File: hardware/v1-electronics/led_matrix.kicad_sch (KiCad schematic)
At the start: 84 parts

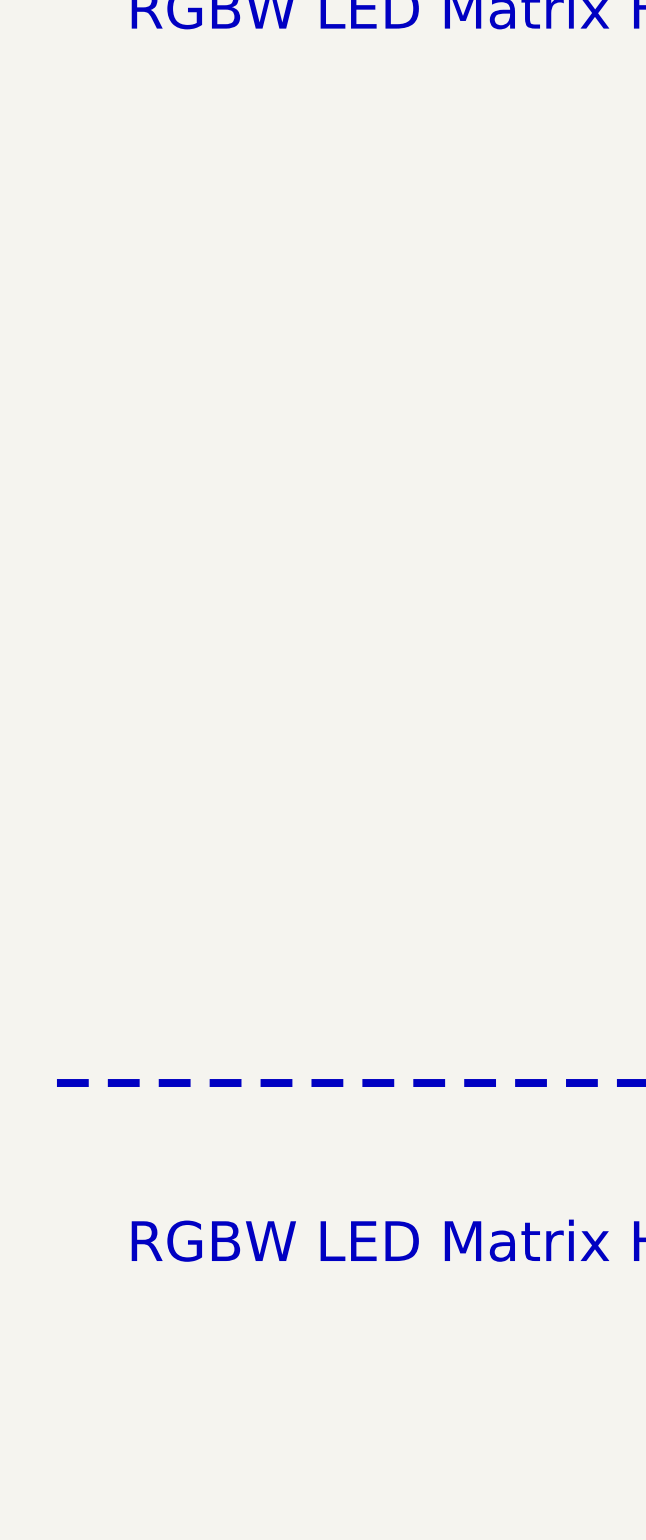
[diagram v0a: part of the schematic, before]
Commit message: refactor(v1 hardware): root level schematic is made discriptive with hierarchical pins
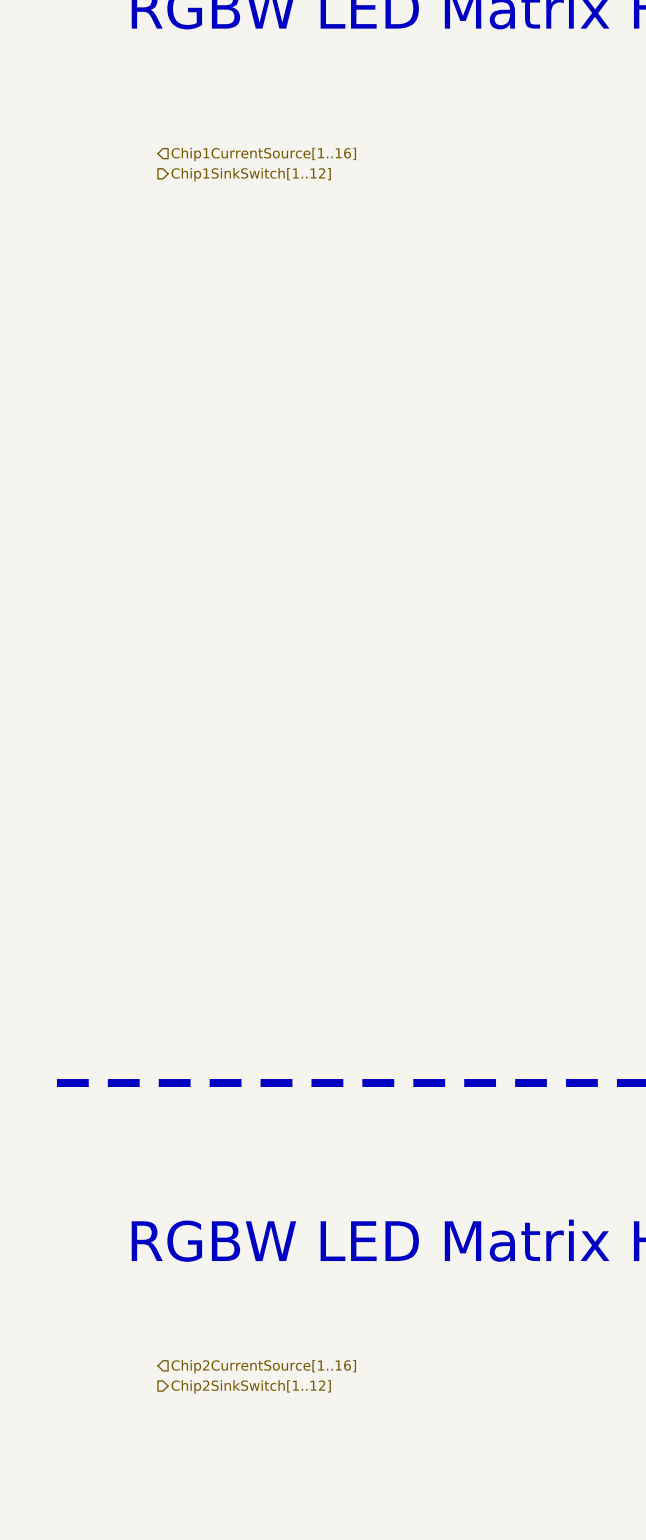
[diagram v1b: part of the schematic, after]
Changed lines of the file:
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@@
+		)
+	)
+	(hierarchical_label "Chip2SinkSwitch[1..12]"
+		(shape output)
+		(at 25.4 205.74 0)
+		(effects
+			(font
+				(size 1.27 1.27)
+			)
+			(justify left)
 		)
 	)
@@
 		)
 	)
+	(hierarchical_label "Chip2CurrentSource[1..16]"
+		(shape input)
+		(at 25.4 203.2 0)
+		(effects
+			(font
+				(size 1.27 1.27)
+			)
+			(justify left)
+		)
+	)
 	(hierarchical_label "CS4_2"
 		(shape input)
@@
 		)
 	)
+	(hierarchical_label "Chip1CurrentSource[1..16]"
+		(shape input)
+		(at 25.4 50.8 0)
+		(effects
+			(font
+				(size 1.27 1.27)
+			)
+			(justify left)
+		)
+	)
 	(hierarchical_label "CS2_1"
 		(shape input)
@@
 		)
 	)
+	(hierarchical_label "Chip1SinkSwitch[1..12]"
+		(shape output)
+		(at 25.4 53.34 0)
+		(effects
+			(font
+				(size 1.27 1.27)
+			)
+			(justify left)
+		)
+	)

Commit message: refactor(v1 hardware): transition to hierarchical pins complete
All the buses renamed to stuff
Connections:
- net CS10_1 renamed Chip1CurrentSource10
- net CS10_2 renamed Chip2CurrentSource10
- net CS11_1 renamed Chip1CurrentSource11
- net CS11_2 renamed Chip2CurrentSource11
- net CS12_1 renamed Chip1CurrentSource12
- net CS12_2 renamed Chip2CurrentSource12
- net CS13_1 renamed Chip1CurrentSource13
- net CS13_2 renamed Chip2CurrentSource13
- net CS14_1 renamed Chip1CurrentSource14
- net CS14_2 renamed Chip2CurrentSource14
- net CS15_1 renamed Chip1CurrentSource15
- net CS15_2 renamed Chip2CurrentSource15
- net CS16_1 renamed Chip1CurrentSource16
- net CS16_2 renamed Chip2CurrentSource16
- net CS1_1 renamed Chip1CurrentSource1
- net CS1_2 renamed Chip2CurrentSource1
- net CS2_1 renamed Chip1CurrentSource2
- net CS2_2 renamed Chip2CurrentSource2
- net CS3_1 renamed Chip1CurrentSource3
- net CS3_2 renamed Chip2CurrentSource3
- net CS4_1 renamed Chip1CurrentSource4
- net CS4_2 renamed Chip2CurrentSource4
- net CS5_1 renamed Chip1CurrentSource5
- net CS5_2 renamed Chip2CurrentSource5
- net CS6_1 renamed Chip1CurrentSource6
- net CS6_2 renamed Chip2CurrentSource6
- net CS7_1 renamed Chip1CurrentSource7
- net CS7_2 renamed Chip2CurrentSource7
- net CS8_1 renamed Chip1CurrentSource8
- net CS8_2 renamed Chip2CurrentSource8
- net CS9_1 renamed Chip1CurrentSource9
- net CS9_2 renamed Chip2CurrentSource9
- net SW10_G_1 renamed Chip1SinkSwitch10
- net SW10_G_2 renamed Chip2SinkSwitch10
- net SW11_R_1 renamed Chip1SinkSwitch11
- net SW11_R_2 renamed Chip2SinkSwitch11
- net SW12_W_1 renamed Chip1SinkSwitch12
- net SW12_W_2 renamed Chip2SinkSwitch12
- net SW1_B_1 renamed Chip1SinkSwitch1
- net SW1_B_2 renamed Chip2SinkSwitch1
- net SW2_G_1 renamed Chip1SinkSwitch2
- net SW2_G_2 renamed Chip2SinkSwitch2
- net SW3_R_1 renamed Chip1SinkSwitch3
- net SW3_R_2 renamed Chip2SinkSwitch3
- net SW4_W_1 renamed Chip1SinkSwitch4
- net SW4_W_2 renamed Chip2SinkSwitch4
- net SW5_B_1 renamed Chip1SinkSwitch5
- net SW5_B_2 renamed Chip2SinkSwitch5
- net SW6_G_1 renamed Chip1SinkSwitch6
- net SW6_G_2 renamed Chip2SinkSwitch6
- net SW7_R_1 renamed Chip1SinkSwitch7
- net SW7_R_2 renamed Chip2SinkSwitch7
- net SW8_W_1 renamed Chip1SinkSwitch8
- net SW8_W_2 renamed Chip2SinkSwitch8
- net SW9_B_1 renamed Chip1SinkSwitch9
- net SW9_B_2 renamed Chip2SinkSwitch9
- no-connect marks 0 -> 24
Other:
- note added: "Blue"
- note added: "Green"
- note added: "Red"
- note added: "White"

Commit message: refactor(v1 hardware): refactored led controllers into a seperate sheet
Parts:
- added JP1: Jumper_2_Open, symbol Jumper:Jumper_2_Open
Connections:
- new net LED Matrix Controller 1/SYNC: JP1.1 (A)
- new net LED Matrix Controller 2/SYNC: JP1.2 (B)
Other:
- added sheet LED Matrix Controller 1 (matric_controller_1.kicad_sch)
- added sheet LED Matrix Controller 2 (matrix_controller_2.kicad_sch)

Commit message: refactor(v1 hardware): get references in order
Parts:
- renumbered LED1_1 to LED1, LED33_2 to LED10, LED2_2 to LED11, LED18_2 to LED12, LED34_2 to LED13, LED3_2 to LED14, LED19_1 to LED15, LED35_1 to LED16, LED4_1 to LED17, LED20_1 to LED18, LED36_1 to LED19, LED17_1 to LED2, LED5_1 to LED20, LED21_1 to LED21, LED19_2 to LED22, LED35_2 to LED23, LED4_2 to LED24, LED20_2 to LED25, LED36_2 to LED26, LED5_2 to LED27, LED21_2 to LED28, LED37_1 to LED29, LED33_1 to LED3, LED6_1 to LED30, LED22_1 to LED31, LED38_1 to LED32, LED7_1 to LED33, LED23_1 to LED34, LED39_1 to LED35, LED37_2 to LED36, LED6_2 to LED37, LED22_2 to LED38, LED38_2 to LED39, LED2_1 to LED4, LED7_2 to LED40, LED23_2 to LED41, LED39_2 to LED42, LED8_1 to LED43, LED24_1 to LED44, LED40_1 to LED45, LED9_1 to LED46, LED25_1 to LED47, LED41_1 to LED48, LED10_1 to LED49, LED18_1 to LED5, LED8_2 to LED50, LED24_2 to LED51, LED40_2 to LED52, LED9_2 to LED53, LED25_2 to LED54, LED41_2 to LED55, LED10_2 to LED56, LED26_1 to LED57, LED42_1 to LED58, LED11_1 to LED59, LED34_1 to LED6, LED27_1 to LED60, LED16_1 to LED61, LED12_1 to LED62, LED28_1 to LED63, LED26_2 to LED66, LED42_2 to LED67, LED11_2 to LED68, LED27_2 to LED69, LED3_1 to LED7, LED16_2 to LED70, LED12_2 to LED71, LED28_2 to LED72, LED32_1 to LED73, LED13_1 to LED74, LED29_1 to LED75, LED15_1 to LED76, LED14_1 to LED77, LED30_1 to LED78, LED31_1 to LED79, LED1_2 to LED8, LED32_2 to LED80, LED13_2 to LED81, LED29_2 to LED82, LED31_2 to LED83, LED14_2 to LED84, LED30_2 to LED85, LED15_2 to LED86, LED17_2 to LED9
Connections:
- net Chip1CurrentSource12: now also LED73.5 (ANODE)
- net Chip1CurrentSource13: now also LED76.5 (ANODE)
- net Chip1CurrentSource14: now also LED79.5 (ANODE)
- net Chip1CurrentSource15: no longer LED76.5 (ANODE), LED79.5 (ANODE)
- net Chip1CurrentSource16: no longer LED61.5 (ANODE), LED73.5 (ANODE)
- net Chip1SinkSwitch1: no longer LED61.1 (BLUE), LED76.1 (BLUE)
- net Chip1SinkSwitch10: now also LED61.2 (GREEN), LED73.2 (GREEN), LED76.2 (GREEN), LED79.2 (GREEN)
- net Chip1SinkSwitch11: now also LED61.3 (RED), LED73.3 (RED), LED76.3 (RED), LED79.3 (RED)
- net Chip1SinkSwitch12: now also LED61.4 (WHITE), LED73.4 (WHITE), LED76.4 (WHITE), LED79.4 (WHITE)
- net Chip1SinkSwitch2: no longer LED61.2 (GREEN), LED76.2 (GREEN)
- net Chip1SinkSwitch3: no longer LED61.3 (RED), LED76.3 (RED)
- net Chip1SinkSwitch4: no longer LED61.4 (WHITE), LED76.4 (WHITE)
- net Chip1SinkSwitch5: no longer LED73.1 (BLUE), LED79.1 (BLUE)
- net Chip1SinkSwitch6: no longer LED73.2 (GREEN), LED79.2 (GREEN)
- net Chip1SinkSwitch7: no longer LED73.3 (RED), LED79.3 (RED)
- net Chip1SinkSwitch8: no longer LED73.4 (WHITE), LED79.4 (WHITE)
- net Chip1SinkSwitch9: now also LED61.1 (BLUE), LED73.1 (BLUE), LED76.1 (BLUE), LED79.1 (BLUE)
- net Chip2CurrentSource11: now also LED70.5 (ANODE)
- net Chip2CurrentSource12: now also LED80.5 (ANODE)
- net Chip2CurrentSource13: now also LED83.5 (ANODE)
- net Chip2CurrentSource14: now also LED86.5 (ANODE)
- net Chip2CurrentSource15: no longer LED83.5 (ANODE), LED86.5 (ANODE)
- net Chip2CurrentSource16: no longer LED70.5 (ANODE), LED80.5 (ANODE)
- net Chip2SinkSwitch1: no longer LED70.1 (BLUE), LED86.1 (BLUE)
- net Chip2SinkSwitch10: now also LED70.2 (GREEN), LED80.2 (GREEN), LED83.2 (GREEN), LED86.2 (GREEN)
- net Chip2SinkSwitch11: now also LED70.3 (RED), LED80.3 (RED), LED83.3 (RED), LED86.3 (RED)
- net Chip2SinkSwitch12: now also LED70.4 (WHITE), LED80.4 (WHITE), LED83.4 (WHITE), LED86.4 (WHITE)
- net Chip2SinkSwitch2: no longer LED70.2 (GREEN), LED86.2 (GREEN)
- net Chip2SinkSwitch3: no longer LED70.3 (RED), LED86.3 (RED)
- net Chip2SinkSwitch4: no longer LED70.4 (WHITE), LED86.4 (WHITE)
- net Chip2SinkSwitch5: no longer LED80.1 (BLUE), LED83.1 (BLUE)
- net Chip2SinkSwitch6: no longer LED80.2 (GREEN), LED83.2 (GREEN)
- net Chip2SinkSwitch7: no longer LED80.3 (RED), LED83.3 (RED)
- net Chip2SinkSwitch8: no longer LED80.4 (WHITE), LED83.4 (WHITE)
- net Chip2SinkSwitch9: now also LED70.1 (BLUE), LED80.1 (BLUE), LED83.1 (BLUE), LED86.1 (BLUE)
- no-connect marks 24 -> 28
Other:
- moved on the sheet: LED61, LED70, LED73, LED76, LED79, LED80, LED83, LED86
